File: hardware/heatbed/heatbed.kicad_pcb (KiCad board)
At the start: 2 copper layers, 80 x 80 mm, 8 parts, among them J1 Conn_01x01, J2 Conn_01x01

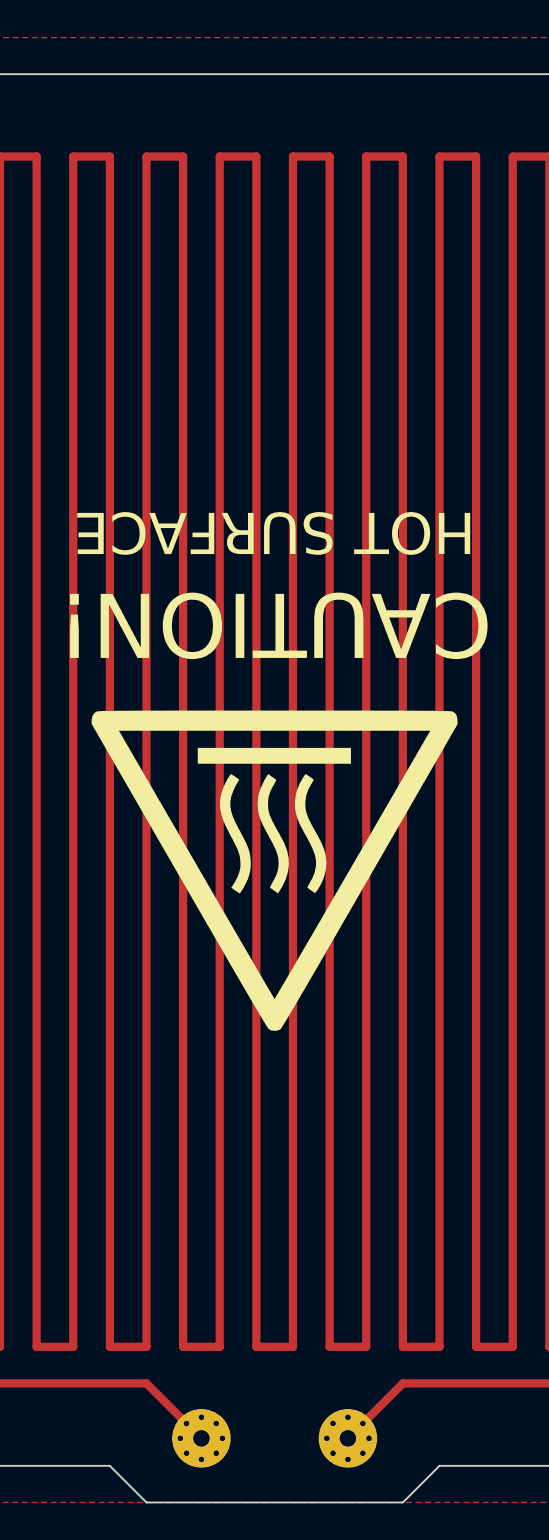
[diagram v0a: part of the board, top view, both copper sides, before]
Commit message: Use one-sided pads
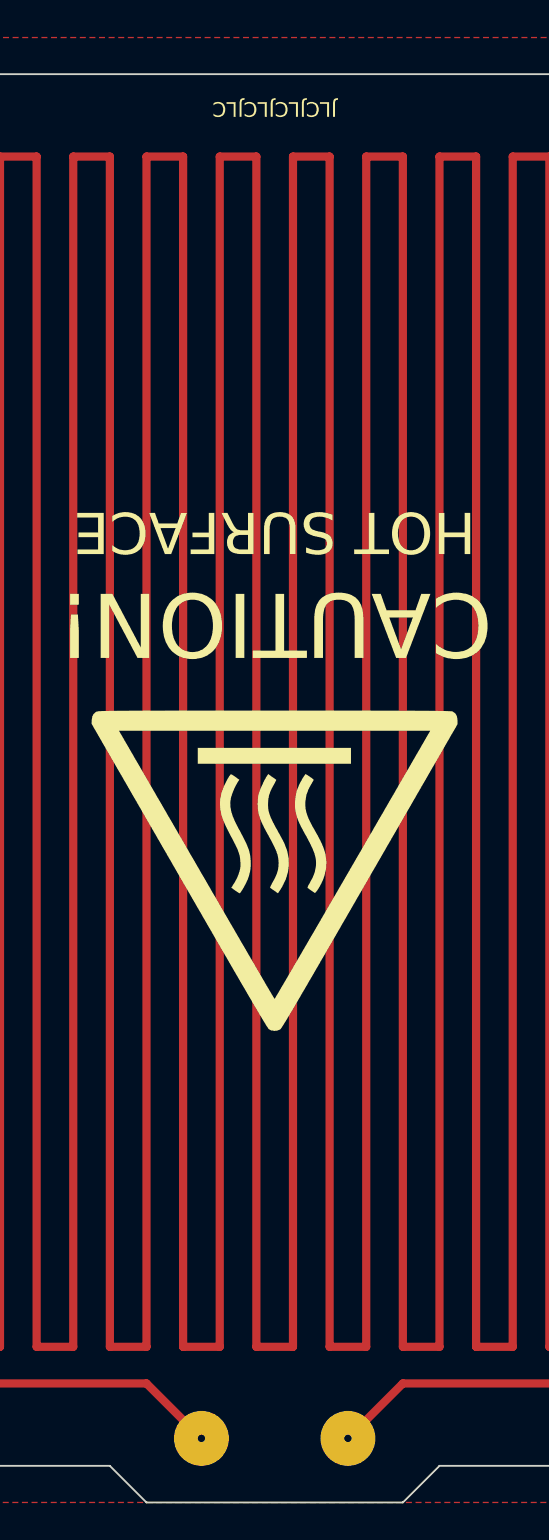
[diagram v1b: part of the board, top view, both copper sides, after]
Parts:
- H1, H2, H3, H4: footprint MountingHole:MountingHole_3mm -> Local_Library:MountingHole_3mm
- J1, J2: footprint Local_Library:Pogo_Pad -> Local_Library:Pad_D3mm_H0.4mm
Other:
- board text added: "JLCJLCJLCJLC"

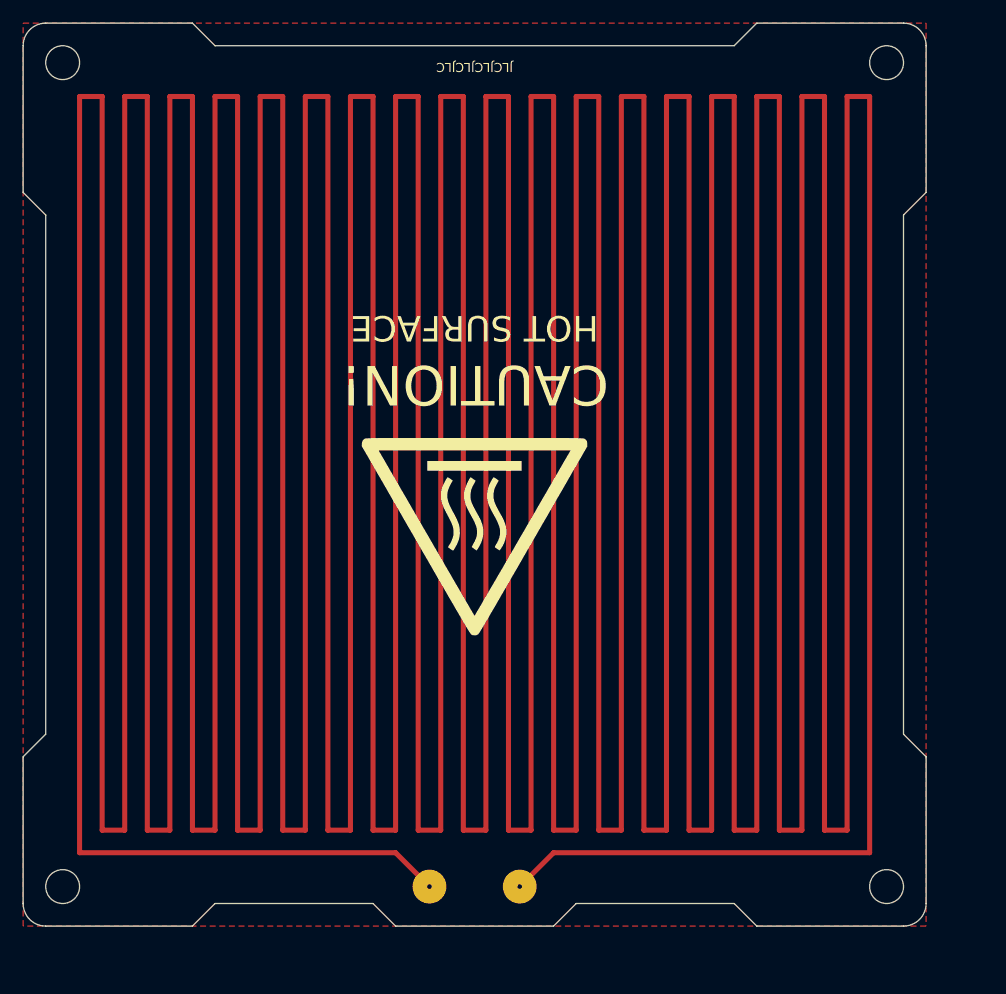
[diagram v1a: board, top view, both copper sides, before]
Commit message: Change mounting holes to M2.5 and use ring terminals
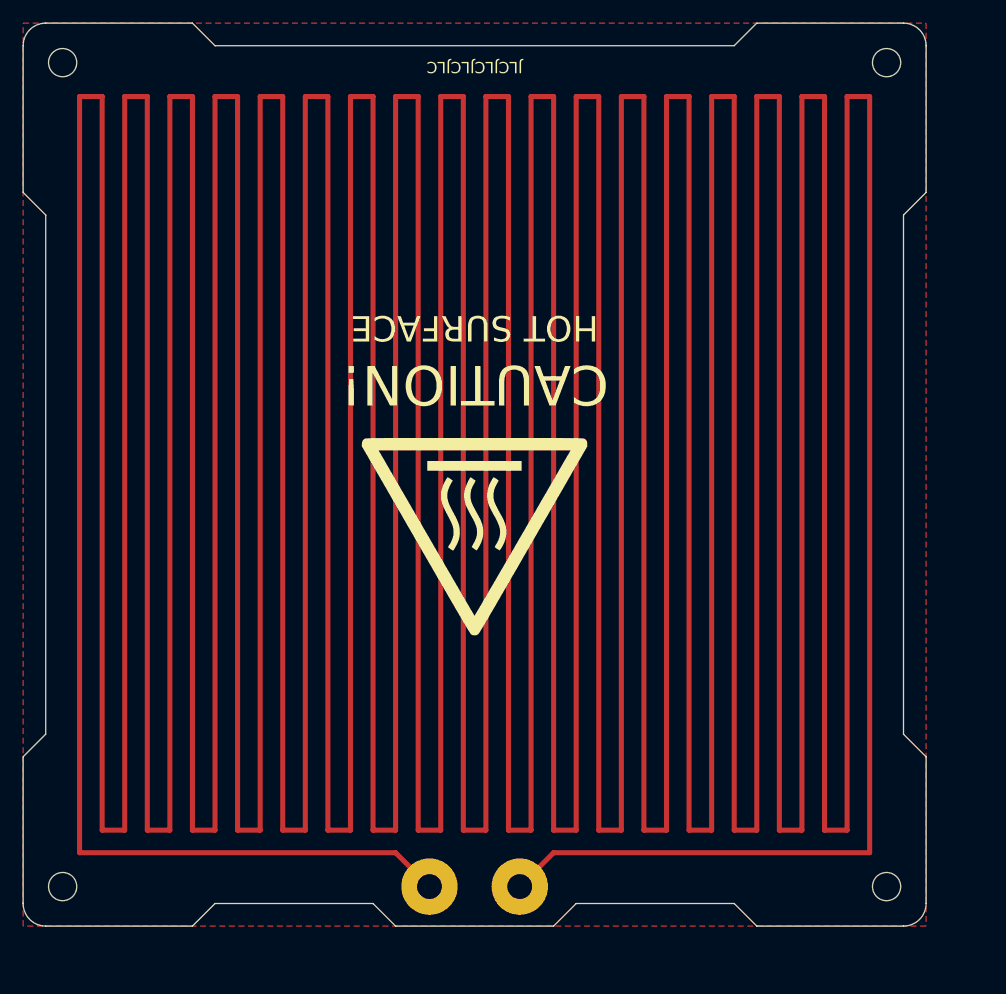
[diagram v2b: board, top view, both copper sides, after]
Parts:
- G*** (x2): footprint Local_Library:Hot_Surface_Sign_20mm -> Local_Library:HotSurfaceSign_20mm
- H1, H2, H3, H4: value 3mm -> 2.5mm; footprint Local_Library:MountingHole_3mm -> Local_Library:MountingHole_2.5mm
- J1, J2: footprint Local_Library:Pad_D3mm_H0.4mm -> Local_Library:Pad_D5mm_H2.2mm
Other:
- board text removed: "THIS SIDE UP"

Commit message: Remove mounting hole silkscreen circles
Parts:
- H1, H2, H3, H4: footprint Local_Library:MountingHole_2.5mm -> MountingHole:MountingHole_2.5mm
- moved H4 109.6 mm to (184.5, 136.5), turned to 180 degrees
- moved H1 104.1 mm to (184.5, 63.5), turned to 180 degrees
- moved H3 102.7 mm to (111.5, 136.5), turned to 180 degrees
- moved H2 96.9 mm to (111.5, 63.5), turned to 180 degrees
- moved J1 70.2 mm to (152.0, 63.5), turned to 180 degrees
- moved J2 69.1 mm to (144.0, 63.5), turned to 180 degrees
- moved G*** 8.60 mm to (148.0, 94.5), turned to 0 degrees
- moved G*** 8.60 mm to (148.0, 94.5), turned to 180 degrees
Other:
- outline, holes or cut-outs redrawn
